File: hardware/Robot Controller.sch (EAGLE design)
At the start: 12 parts

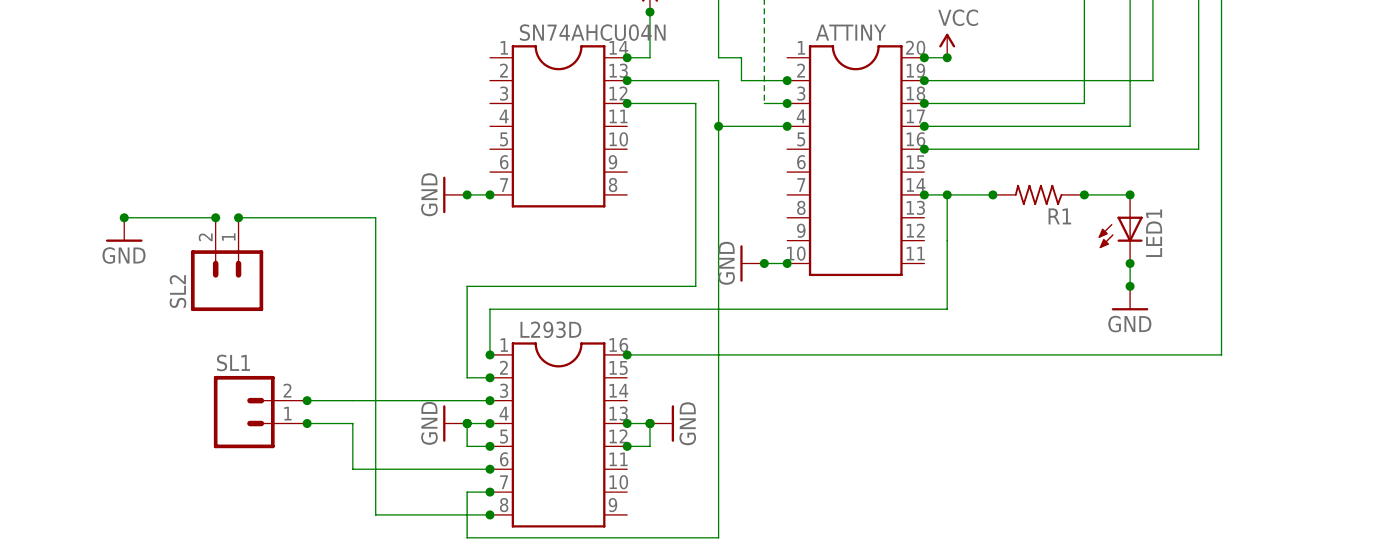
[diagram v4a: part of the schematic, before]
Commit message: update hardware for second motor
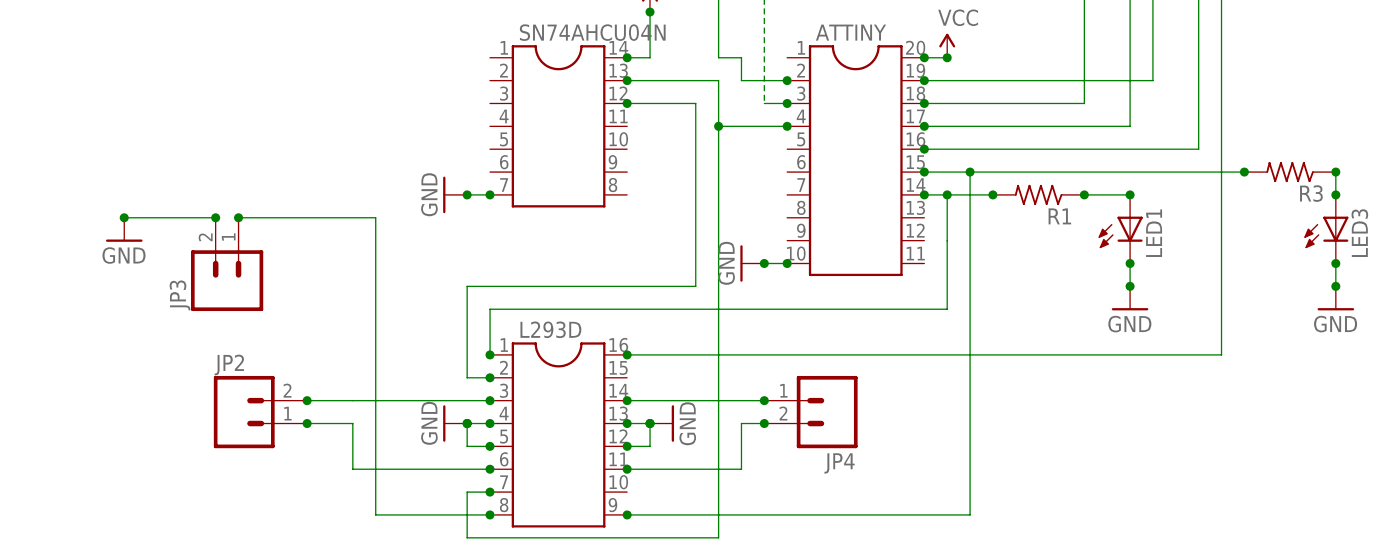
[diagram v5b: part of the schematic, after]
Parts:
- removed SL1, SL2: (no value), con-amp-quick:M02
- added JP2, JP3, JP4: (no value), SparkFun-Connectors:M025MM
- added LED3: (no value), led:LEDSMT1206
- added R3: (no value), resistor:R-US_R3216
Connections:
- new net N$11: ATTINY.15, L293D.9, R3.2
- new net N$14: LED3.A, R3.1
- new net N$18: JP4.1, L293D.14
- new net N$19: JP4.2, L293D.11
- net GND: now also JP3.2, LED3.C; no longer SL2.2
- net N$10: now also JP3.1; no longer SL2.1
- net N$8: now also JP2.2; no longer SL1.2
- net N$9: now also JP2.1; no longer SL1.1
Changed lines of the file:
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@@
 <part name="R1" library="resistor" deviceset="R-US_" device="R3216"/>
 <part name="LED1" library="led" deviceset="LED" device="SMT1206"/>
-<part name="SL1" library="con-amp-quick" deviceset="M02" device=""/>
-<part name="SL2" library="con-amp-quick" deviceset="M02" device=""/>
 <part name="H1" library="holes" deviceset="MOUNT-HOLE" device="2.8"/>
 <part name="H2" library="holes" deviceset="MOUNT-HOLE" device="2.8"/>
+<part name="R3" library="resistor" deviceset="R-US_" device="R3216"/>
+<part name="LED3" library="led" deviceset="LED" device="SMT1206"/>
+<part name="GND9" library="SparkFun-Aesthetics" deviceset="GND" device=""/>
+<part name="JP2" library="SparkFun-Connectors" deviceset="M02" device="5MM"/>
+<part name="JP3" library="SparkFun-Connectors" deviceset="M02" device="5MM"/>
+<part name="JP4" library="SparkFun-Connectors" deviceset="M02" device="5MM"/>
 </parts>
 <sheets>
@@
 <instance part="R1" gate="G$1" x="78.74" y="58.42" rot="R180"/>
 <instance part="LED1" gate="G$1" x="88.9" y="55.88"/>
-<instance part="SL1" gate="G$1" x="-10.16" y="33.02"/>
-<instance part="SL2" gate="G$1" x="-10.16" y="48.26" rot="R90"/>
 <instance part="H1" gate="G$1" x="-35.56" y="114.3"/>
 <instance part="H2" gate="G$1" x="-35.56" y="106.68"/>
+<instance part="R3" gate="G$1" x="106.68" y="60.96" rot="R180"/>
+<instance part="LED3" gate="G$1" x="111.76" y="55.88"/>
+<instance part="GND9" gate="1" x="111.76" y="45.72"/>
+<instance part="JP2" gate="G$1" x="-10.16" y="33.02"/>
+<instance part="JP3" gate="G$1" x="-10.16" y="48.26" rot="R90"/>
+<instance part="JP4" gate="G$1" x="55.88" y="35.56" rot="R180"/>
 </instances>
 <busses>
@@
 <wire x1="2.54" y1="35.56" x2="17.78" y2="35.56" width="0.1524" layer="91"/>
 <junction x="17.78" y="35.56"/>
-<pinref part="SL1" gate="G$1" pin="2"/>
 <wire x1="2.54" y1="35.56" x2="-2.54" y2="35.56" width="0.1524" layer="91"/>
+<pinref part="JP2" gate="G$1" pin="2"/>
 <junction x="-2.54" y="35.56"/>
 </segment>
@@
 <junction x="17.78" y="27.94"/>
 <wire x1="2.54" y1="27.94" x2="2.54" y2="33.02" width="0.1524" layer="91"/>
-<pinref part="SL1" gate="G$1" pin="1"/>
 <wire x1="2.54" y1="33.02" x2="-2.54" y2="33.02" width="0.1524" layer="91"/>
+<pinref part="JP2" gate="G$1" pin="1"/>
 <junction x="-2.54" y="33.02"/>
 </segment>
@@
 <wire x1="5.08" y1="22.86" x2="17.78" y2="22.86" width="0.1524" layer="91"/>
 <junction x="17.78" y="22.86"/>
-<pinref part="SL2" gate="G$1" pin="1"/>
+<pinref part="JP3" gate="G$1" pin="1"/>
 <junction x="-10.16" y="55.88"/>
 </segment>
@@
 <wire x1="-22.86" y1="55.88" x2="-12.7" y2="55.88" width="0.1524" layer="91"/>
 <junction x="-22.86" y="55.88"/>
-<pinref part="SL2" gate="G$1" pin="2"/>
+<pinref part="JP3" gate="G$1" pin="2"/>
 <junction x="-12.7" y="55.88"/>
 </segment>
@@
 <junction x="43.18" y="109.22"/>
 <junction x="43.18" y="111.76"/>
+</segment>
+<segment>
+<pinref part="LED3" gate="G$1" pin="C"/>
+<pinref part="GND9" gate="1" pin="GND"/>
+<wire x1="111.76" y1="50.8" x2="111.76" y2="48.26" width="0.1524" layer="91"/>
+<junction x="111.76" y="50.8"/>
+<junction x="111.76" y="48.26"/>
 </segment>
 </net>
@@
 </segment>
 </net>
+<net name="N$11" class="0">
+<segment>
+<pinref part="ATTINY" gate="G$1" pin="15"/>
+<wire x1="66.04" y1="60.96" x2="71.12" y2="60.96" width="0.1524" layer="91"/>
+<wire x1="71.12" y1="60.96" x2="71.12" y2="22.86" width="0.1524" layer="91"/>
+<pinref part="L293D" gate="G$1" pin="9"/>
+<wire x1="71.12" y1="22.86" x2="33.02" y2="22.86" width="0.1524" layer="91"/>
+<junction x="33.02" y="22.86"/>
+<junction x="66.04" y="60.96"/>
+<pinref part="R3" gate="G$1" pin="2"/>
+<wire x1="71.12" y1="60.96" x2="101.6" y2="60.96" width="0.1524" layer="91"/>
+<junction x="71.12" y="60.96"/>
+<junction x="101.6" y="60.96"/>
+</segment>
+</net>
+<net name="N$14" class="0">
+<segment>
+<pinref part="R3" gate="G$1" pin="1"/>
+<pinref part="LED3" gate="G$1" pin="A"/>
+<wire x1="111.76" y1="60.96" x2="111.76" y2="58.42" width="0.1524" layer="91"/>
+<junction x="111.76" y="60.96"/>
+<junction x="111.76" y="58.42"/>
+</segment>
+</net>
+<net name="N$18" class="0">
+<segment>
+<pinref part="L293D" gate="G$1" pin="14"/>
+<pinref part="JP4" gate="G$1" pin="1"/>
+<wire x1="33.02" y1="35.56" x2="48.26" y2="35.56" width="0.1524" layer="91"/>
+<junction x="48.26" y="35.56"/>
+<junction x="33.02" y="35.56"/>
+</segment>
+</net>
+<net name="N$19" class="0">
+<segment>
+<pinref part="L293D" gate="G$1" pin="11"/>
+<wire x1="33.02" y1="27.94" x2="45.72" y2="27.94" width="0.1524" layer="91"/>
+<wire x1="45.72" y1="27.94" x2="45.72" y2="33.02" width="0.1524" layer="91"/>
+<pinref part="JP4" gate="G$1" pin="2"/>
+<wire x1="45.72" y1="33.02" x2="48.26" y2="33.02" width="0.1524" layer="91"/>
+<junction x="48.26" y="33.02"/>
+<junction x="33.02" y="27.94"/>
+</segment>
+</net>

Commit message: ideas around master/slave robot cores
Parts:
- added JP5, JP6: (no value), pinhead:PINHD-1X7
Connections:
- net GND: now also JP5.6
- net N$12: now also JP5.1
- net N$4: now also JP5.2
- net N$5: now also JP5.4
- net N$7: now also JP5.3
- net VCC: now also JP5.7
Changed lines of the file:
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@@
 <part name="JP3" library="SparkFun-Connectors" deviceset="M02" device="5MM"/>
 <part name="JP4" library="SparkFun-Connectors" deviceset="M02" device="5MM"/>
+<part name="JP5" library="pinhead" deviceset="PINHD-1X7" device=""/>
+<part name="JP6" library="pinhead" deviceset="PINHD-1X7" device=""/>
+<part name="GND10" library="SparkFun-Aesthetics" deviceset="GND" device=""/>
+<part name="SUPPLY4" library="SparkFun-Aesthetics" deviceset="VCC" device=""/>
 </parts>
 <sheets>
@@
 <instance part="JP3" gate="G$1" x="-10.16" y="48.26" rot="R90"/>
 <instance part="JP4" gate="G$1" x="55.88" y="35.56" rot="R180"/>
+<instance part="JP5" gate="A" x="111.76" y="99.06" rot="R90"/>
+<instance part="JP6" gate="A" x="-25.4" y="71.12" rot="R180"/>
+<instance part="GND10" gate="1" x="116.84" y="78.74"/>
+<instance part="SUPPLY4" gate="1" x="121.92" y="86.36" rot="R180"/>
 </instances>
 <busses>
@@
 <pinref part="ATTINY" gate="G$1" pin="16"/>
 <wire x1="66.04" y1="63.5" x2="96.52" y2="63.5" width="0.1524" layer="91"/>
-<wire x1="96.52" y1="63.5" x2="96.52" y2="101.6" width="0.1524" layer="91"/>
+<wire x1="96.52" y1="63.5" x2="96.52" y2="88.9" width="0.1524" layer="91"/>
+<wire x1="96.52" y1="88.9" x2="96.52" y2="101.6" width="0.1524" layer="91"/>
 <wire x1="96.52" y1="101.6" x2="96.52" y2="109.22" width="0.1524" layer="91"/>
 <pinref part="JP1" gate="A" pin="24"/>
@@
 <junction x="83.82" y="101.6"/>
 <junction x="66.04" y="63.5"/>
+<wire x1="96.52" y1="88.9" x2="106.68" y2="88.9" width="0.1524" layer="91"/>
+<pinref part="JP5" gate="A" pin="2"/>
+<wire x1="106.68" y1="88.9" x2="106.68" y2="96.52" width="0.1524" layer="91"/>
+<junction x="96.52" y="88.9"/>
+<junction x="106.68" y="96.52"/>
 </segment>
 </net>
@@
 <junction x="66.04" y="66.04"/>
 <junction x="78.74" y="93.98"/>
+<pinref part="JP5" gate="A" pin="4"/>
+<wire x1="111.76" y1="96.52" x2="111.76" y2="83.82" width="0.1524" layer="91"/>
+<wire x1="111.76" y1="83.82" x2="88.9" y2="83.82" width="0.1524" layer="91"/>
+<junction x="88.9" y="83.82"/>
+<junction x="111.76" y="96.52"/>
 </segment>
 </net>
@@
 <wire x1="83.82" y1="93.98" x2="83.82" y2="91.44" width="0.1524" layer="91"/>
 <wire x1="83.82" y1="91.44" x2="91.44" y2="91.44" width="0.1524" layer="91"/>
-<wire x1="91.44" y1="91.44" x2="91.44" y2="71.12" width="0.1524" layer="91"/>
+<wire x1="91.44" y1="91.44" x2="91.44" y2="86.36" width="0.1524" layer="91"/>
 <pinref part="ATTINY" gate="G$1" pin="19"/>
+<wire x1="91.44" y1="86.36" x2="91.44" y2="71.12" width="0.1524" layer="91"/>
 <wire x1="91.44" y1="71.12" x2="66.04" y2="71.12" width="0.1524" layer="91"/>
 <junction x="83.82" y="93.98"/>
 <junction x="66.04" y="71.12"/>
+<pinref part="JP5" gate="A" pin="3"/>
+<wire x1="91.44" y1="86.36" x2="109.22" y2="86.36" width="0.1524" layer="91"/>
+<wire x1="109.22" y1="86.36" x2="109.22" y2="96.52" width="0.1524" layer="91"/>
+<junction x="91.44" y="86.36"/>
+<junction x="109.22" y="96.52"/>
 </segment>
 </net>
@@
 <wire x1="55.88" y1="111.76" x2="55.88" y2="114.3" width="0.1524" layer="91"/>
 <wire x1="55.88" y1="114.3" x2="99.06" y2="114.3" width="0.1524" layer="91"/>
-<wire x1="99.06" y1="114.3" x2="99.06" y2="40.64" width="0.1524" layer="91"/>
+<wire x1="99.06" y1="114.3" x2="99.06" y2="91.44" width="0.1524" layer="91"/>
 <pinref part="L293D" gate="G$1" pin="16"/>
+<wire x1="99.06" y1="91.44" x2="99.06" y2="40.64" width="0.1524" layer="91"/>
 <wire x1="99.06" y1="40.64" x2="33.02" y2="40.64" width="0.1524" layer="91"/>
 <junction x="33.02" y="40.64"/>
 <junction x="55.88" y="101.6"/>
+<pinref part="JP5" gate="A" pin="1"/>
+<wire x1="104.14" y1="96.52" x2="104.14" y2="91.44" width="0.1524" layer="91"/>
+<wire x1="104.14" y1="91.44" x2="99.06" y2="91.44" width="0.1524" layer="91"/>
+<junction x="99.06" y="91.44"/>
+<junction x="104.14" y="96.52"/>
 </segment>
 </net>
@@
 <junction x="111.76" y="48.26"/>
 </segment>
+<segment>
+<pinref part="JP5" gate="A" pin="6"/>
+<pinref part="GND10" gate="1" pin="GND"/>
+<wire x1="116.84" y1="96.52" x2="116.84" y2="81.28" width="0.1524" layer="91"/>
+<junction x="116.84" y="81.28"/>
+<junction x="116.84" y="96.52"/>
+</segment>
 </net>
 <net name="VCC" class="0">
@@
 <junction x="35.56" y="78.74"/>
 </segment>
-</net>
+<segment>
+<pinref part="JP5" gate="A" pin="7"/>
+<wire x1="119.38" y1="96.52" x2="119.38" y2="88.9" width="0.1524" layer="91"/>
+<pinref part="SUPPLY4" gate="1" pin="VCC"/>
+<wire x1="119.38" y1="88.9" x2="121.92" y2="88.9" width="0.1524" layer="91"/>
+<wire x1="121.92" y1="88.9" x2="121.92" y2="86.36" width="0.1524" layer="91"/>
+<junction x="121.92" y="86.36"/>
+<junction x="119.38" y="96.52"/>
+</segment>
+</net>

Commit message: WIP dev board
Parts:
- removed H2: MOUNT-HOLE2.8, holes:MOUNT-HOLE2.8
- added JP8: (no value), pinhead:PINHD-1X10
- added S1: (no value), switch-omron:10-XX
- JP6: device pinhead:PINHD-1X7 -> pinhead:PINHD-1X3
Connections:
- new net N$20: ATTINY.5, L293D.10, SN74AHCU04N.11
- new net N$21: JP6.1, R2.1
- new net N$22: L293D.15, SN74AHCU04N.10
- new net N$23: JP6.3, JP8.8
- new net N$24: ATTINY.6, JP8.7
- new net N$25: ATTINY.7, JP8.6
- new net N$26: ATTINY.8, JP8.5
- new net N$27: ATTINY.9, JP8.4
- new net N$28: ATTINY.13, JP8.1
- new net N$29: ATTINY.12, JP8.2
- new net N$30: ATTINY.11, JP8.3
- new net N$31: ATTINY.1, S1.P
- net GND: now also JP8.10, S1.S1
- net N$16: now also JP6.2; no longer R2.1
- net VCC: now also JP8.9
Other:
- moved on the sheet: JP4, LED2, R2, SN74AHCU04N

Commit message: silkscreen work
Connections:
- net N$6: now also JP5.5
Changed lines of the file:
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@@
 <junction x="81.28" y="93.98"/>
 <junction x="66.04" y="68.58"/>
+<pinref part="JP5" gate="A" pin="5"/>
+<wire x1="83.82" y1="81.28" x2="114.3" y2="81.28" width="0.1524" layer="91"/>
+<wire x1="114.3" y1="81.28" x2="114.3" y2="96.52" width="0.1524" layer="91"/>
+<junction x="83.82" y="81.28"/>
+<junction x="114.3" y="96.52"/>
 </segment>
 </net>
